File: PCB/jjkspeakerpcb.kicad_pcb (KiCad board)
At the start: 2 copper layers, 99.3 x 99.3 mm, 19 parts, among them J1 TFT 8PIN, SW1 UP, SW2 DOWN, SW3 TIME SET, SW4 CLOCK SET, SW5 SNOOZE, SW6 ALARM ON, U1 XIAO ESP32-C3

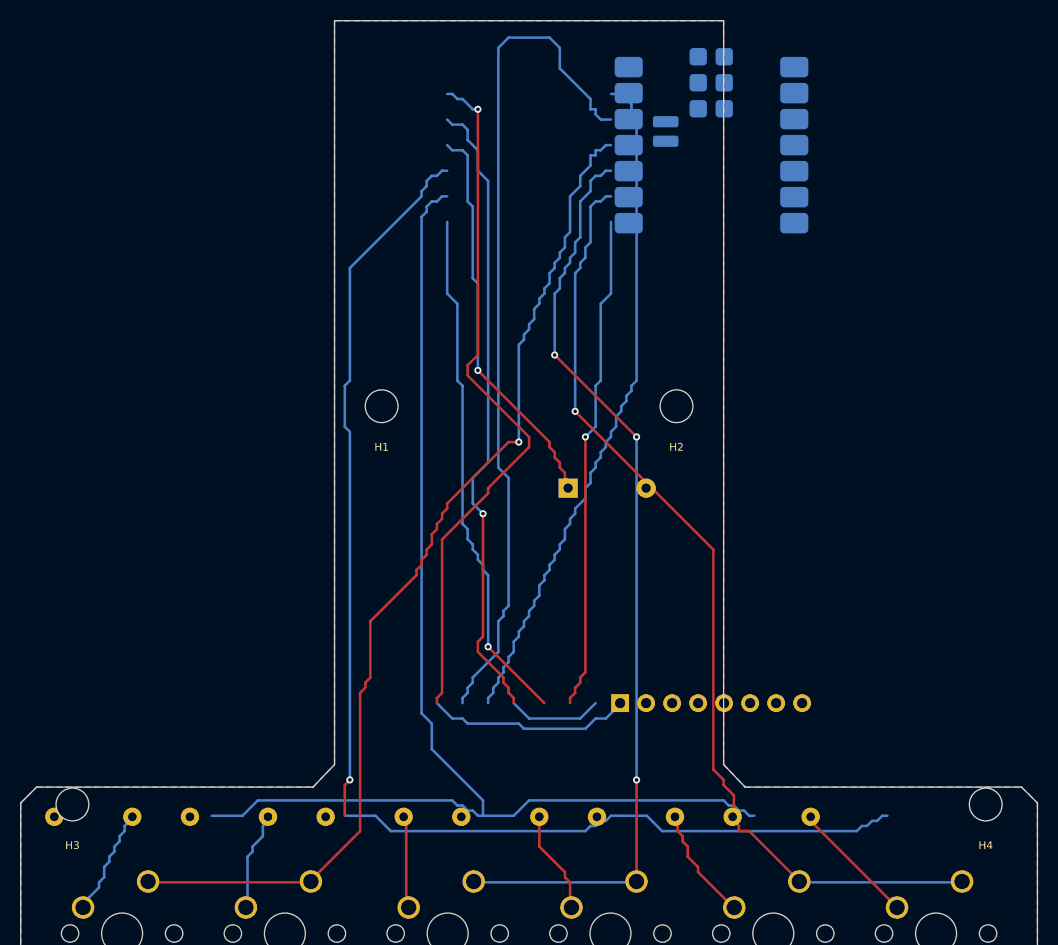
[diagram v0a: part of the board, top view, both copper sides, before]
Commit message: GGK Alarm Rev D: validated KiCad layout, firmware, safety gates and full build guide
* Add detailed native PCB parser diagnostics to Rev D audit gate

* Bisect native KiCad file parsing to identify invalid PCB S-expressions

* Repair malformed GND zone syntax and correct 1N4148 schematic orientation note

* Rebuild native KiCad from corrected B-side coordinates; remove overlapping holes, align schematic and nets

* Fix backside fab text mirror and regenerate local KiCad libraries for native ERC/DRC

* Diagnose remaining XIAO KiCad library mismatch using actual pcbnew geometry

* Reconstruct XIAO rear module from canonical front footprint with genuine mirrored SMD pads

* Isolate XIAO library shape mismatch: retain canonical 22 pad layout, remove redundant rear component graphics

* Correct underside pad mirroring; enforce native pad parity; regenerate board in CI

* Correct KiCad back-side pad positions and diode pin geometry using native observations

* Regenerate PCB and schematic using KiCad backside coordinates

* Fix XIAO local library mirroring to match audited board pad geometry

* Audit exact XIAO library footprint comparison using native pcbnew

* Regenerate PCB and schematic using KiCad backside coordinates

* Bundle XIAO as an exact native backside KiCad footprint for DRC comparison

* Regenerate PCB and schematic using KiCad backside coordinates

* Finish Rev D gate: filled GND zones, clean ERC DRC, real Arduino compile evidence

* Add no-extra-parts timer and stopwatch with overflow-safe tests and portrait UI

* Resolve native filled-zone thermal DRC at TFT J1 ground pad

* Regenerate PCB and schematic using KiCad backside coordinates

* Finalize Rev D evidence, verified BOM mounting, safe power guidance and release hold

* Retain mandatory DESIGN HOLD state while recording passing native KiCad checks

* Add native-KiCad verified design source synchronization before PR merge

* Restore known-good KiCad board generator and fix outdated Tinkercad SVG hole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
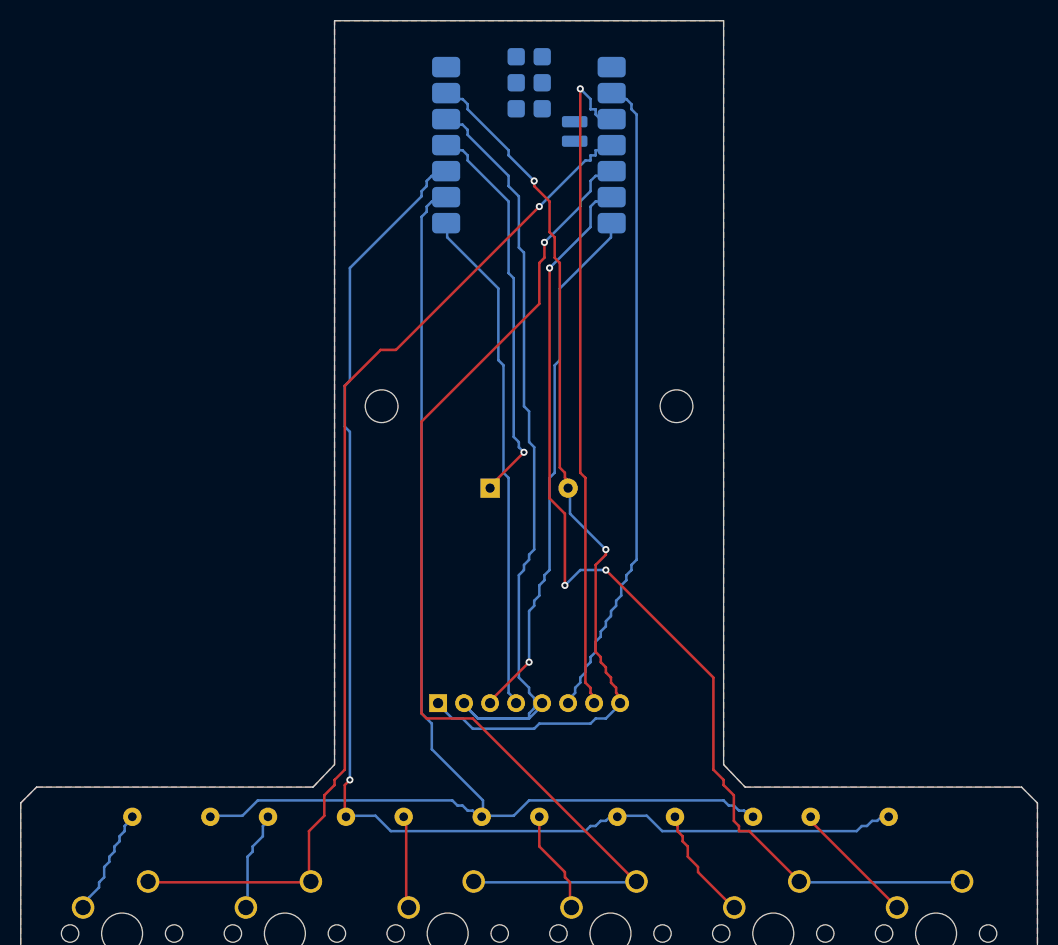
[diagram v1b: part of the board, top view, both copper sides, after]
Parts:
- removed the H1 at (35.6, 38.0)
- removed H3, H4: M3, GGK:MountingHole_3.2
- added BZ1: 3.3V PIEZO, GGK:Piezo_P12_P7.62, B.Cu at (46.2, 46.0)
- H1: renamed from BZ1; value 3.3V PIEZO -> M3; footprint GGK:Piezo_P12_P7.62 -> GGK:MountingHole_3.2; moved to F.Cu
- moved H1 19.9 mm to (35.6, 38.0)
- moved J1 17.8 mm to (41.1, 67.0)
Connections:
- net 3V3 renamed /3V3
- net COL_BOTTOM renamed /COL_BOTTOM
- net COL_MIDDLE renamed /COL_MIDDLE
- net COL_TOP renamed /COL_TOP
- net DISP_CS renamed /DISP_CS
- net DISP_DC renamed /DISP_DC
- net DISP_MOSI renamed /DISP_MOSI
- net DISP_SCK renamed /DISP_SCK
- net K1 renamed /K1
- net K2 renamed /K2
- net K3 renamed /K3
- net K4 renamed /K4
- net K5 renamed /K5
- net K6 renamed /K6
- net ROW_LEFT renamed /ROW_LEFT
- net ROW_RIGHT renamed /ROW_RIGHT
- J1 pad 1: GND -> /GND
- J1 pad 8: GND -> /GND
- U1 pad 11: PIEZO -> /PIEZO
- U1 pad 13: GND -> /GND
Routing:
- net GND: track 88.3 -> 0.00 mm, vias 1 -> 0
- net /GND: track 0.00 -> 88.0 mm, vias 0 -> 2
- net PIEZO: track 39.1 -> 0.00 mm, vias 1 -> 0
- net /PIEZO: track 0.00 -> 38.6 mm, vias 0 -> 1
- net /DISP_CS: track 83.1 -> 65.7 mm, vias 0 -> 1
- net /COL_MIDDLE: track 91.7 -> 105.1 mm, vias 3 -> 1
- net /3V3: track 71.2 -> 80.4 mm, vias 1 -> 0
- net /COL_BOTTOM: track 94.7 -> 101.3 mm, vias 1 -> 3
- net /DISP_SCK: track 48.7 -> 52.0 mm
- net /DISP_DC: track 67.1 -> 63.8 mm
- net /DISP_MOSI: track 50.9 -> 49.7 mm, vias 1 -> 0
- net /COL_TOP: track 101.2 -> 101.8 mm
- added copper zone on B.Cu, net /GND
- added copper zone on F.Cu, net /GND
- removed copper zone on B.Cu, net GND
- removed copper zone on F.Cu, net GND
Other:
- board text added: "6 KEY MATRIX / PORTRAIT TFT"
- board text added: "GGK ALARM REV D"
- board text removed: "6 KEY MATRIX // TFT ON FRONT"
- board text removed: "GGK ALARM R2"

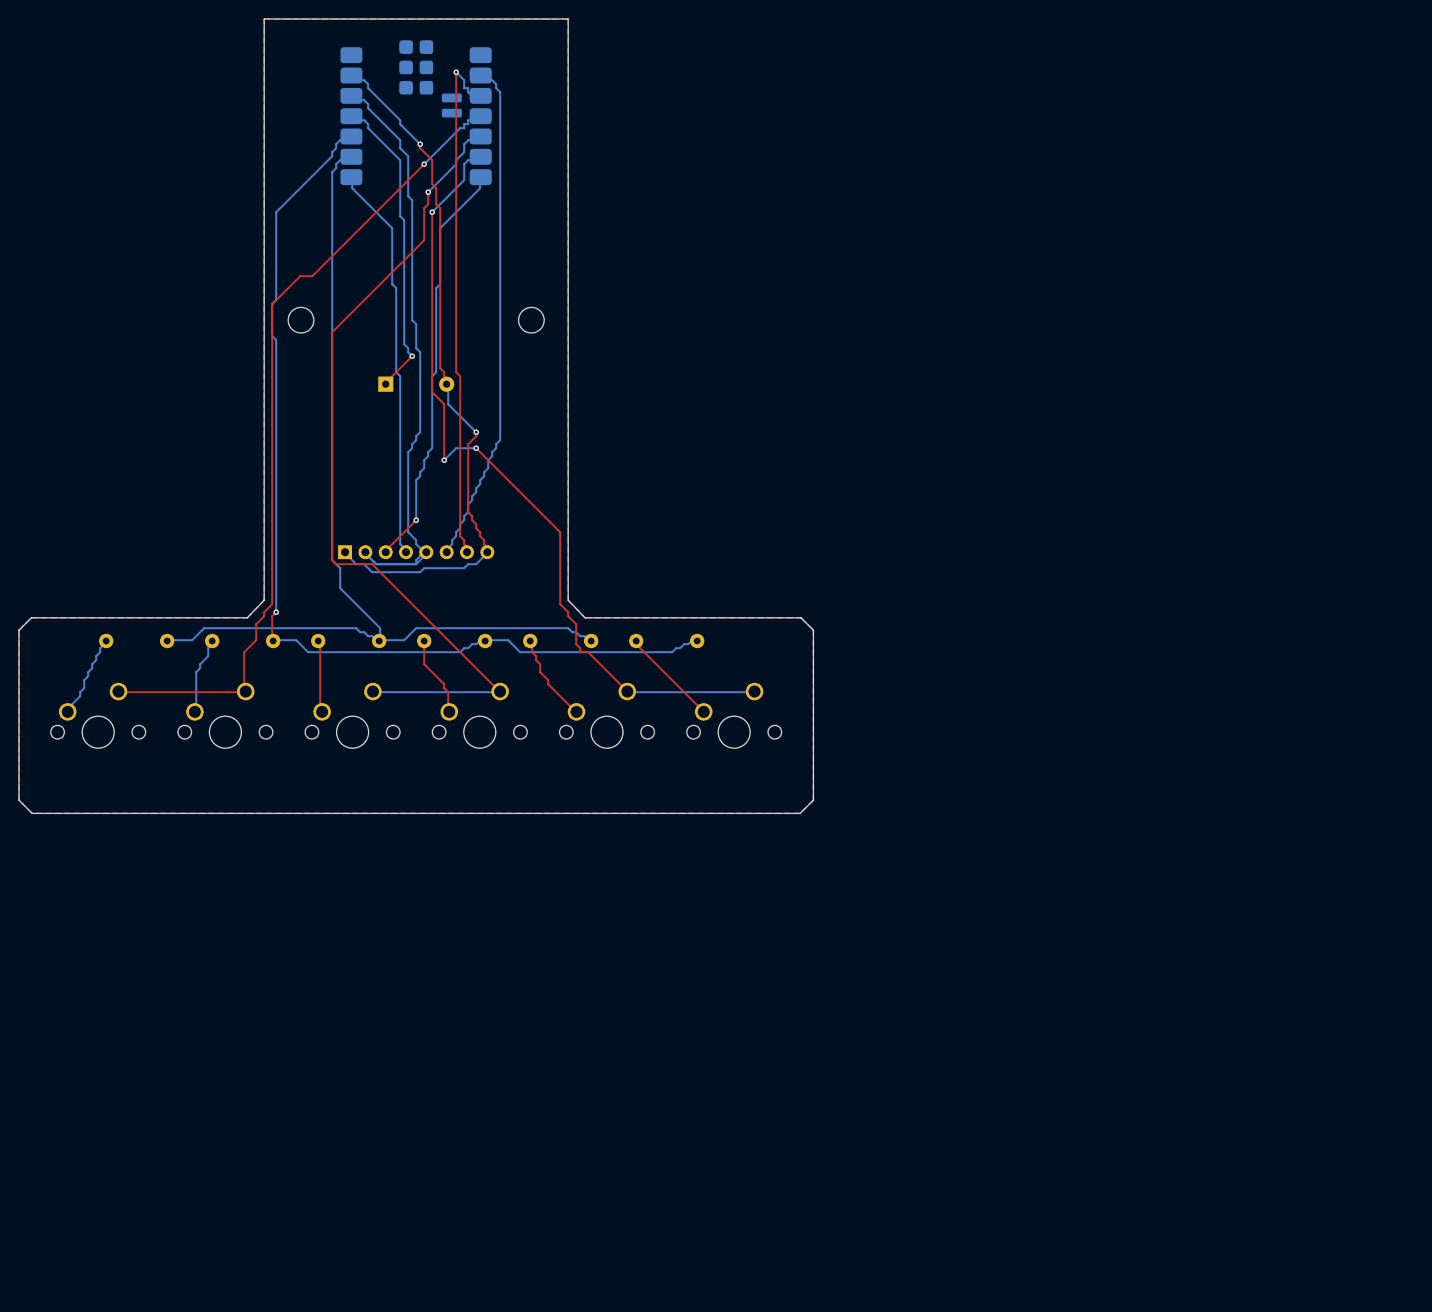
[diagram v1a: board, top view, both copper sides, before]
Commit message: Stage rectangular BLARE KiCad sources, screenshots, and incomplete Gerbers (README held)
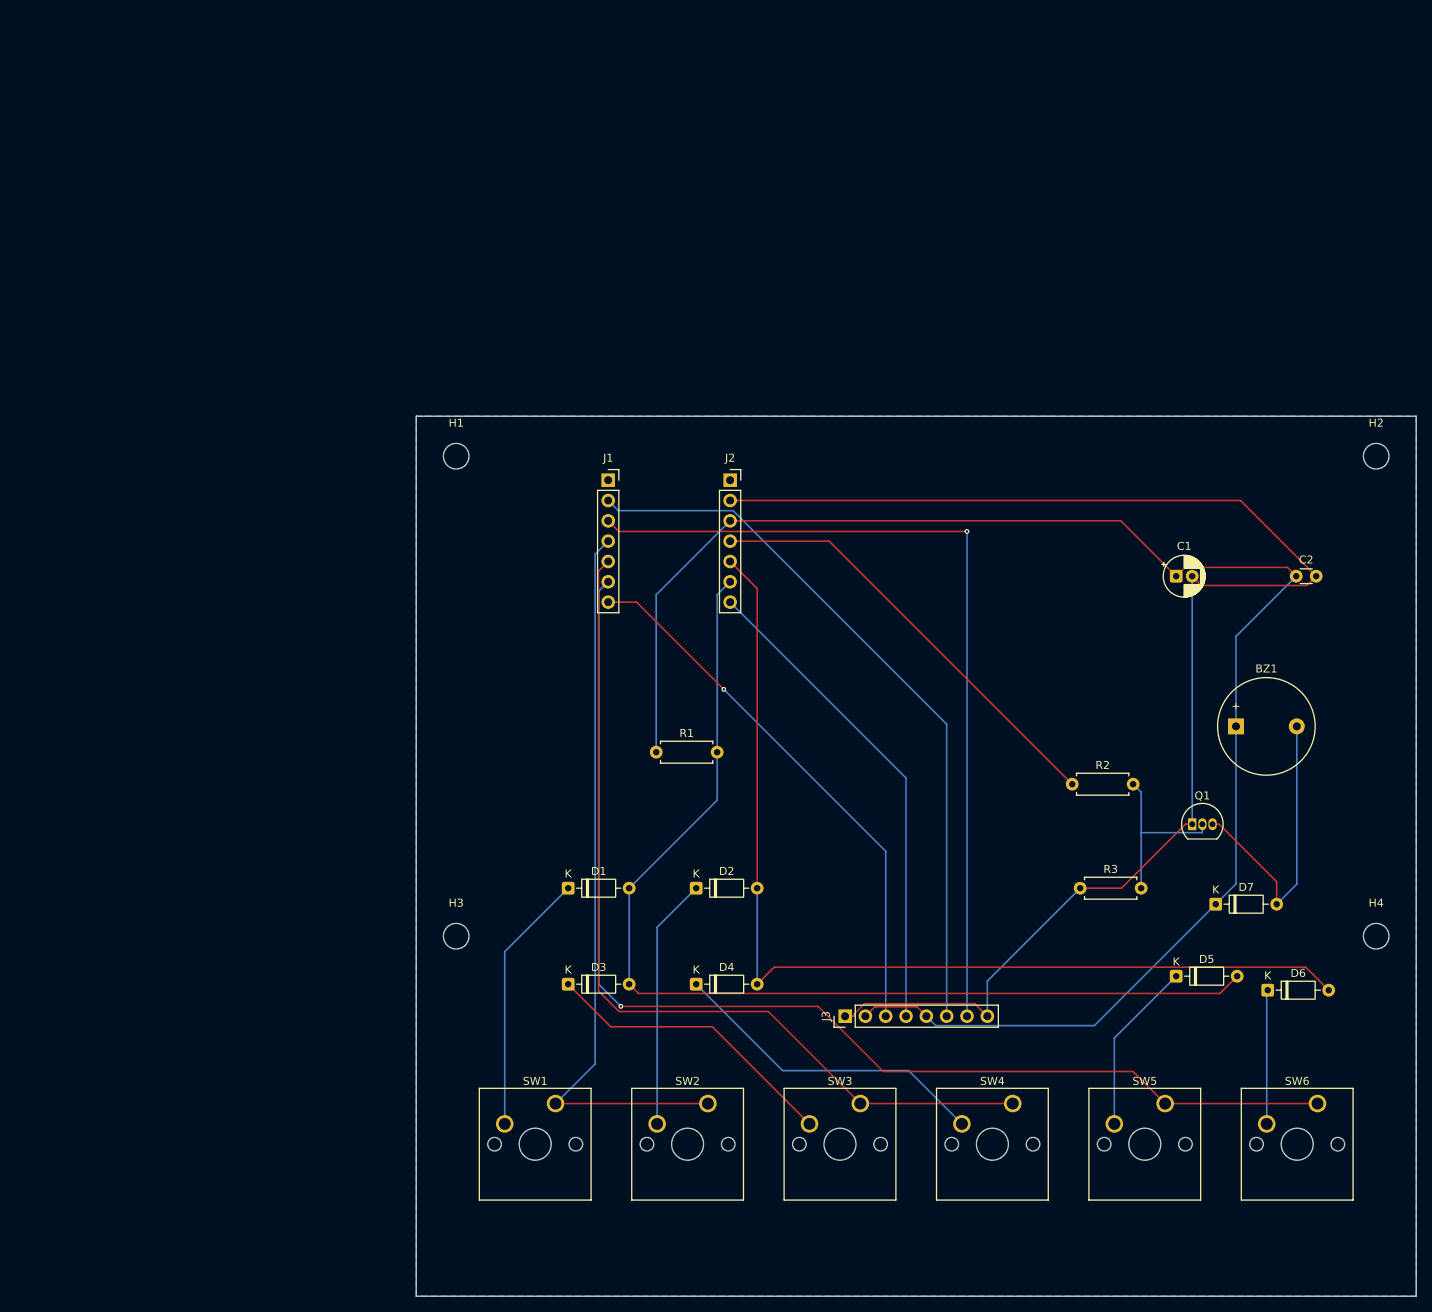
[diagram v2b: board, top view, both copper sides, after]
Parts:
- removed U1: XIAO ESP32-C3, GGK:Seeed_XIAO_ESP32C3_Castellated
- added C1: 10uF, Capacitor_THT:CP_Radial_D5.0mm_P2.00mm, F.Cu at (145.0, 70.0)
- added C2: 100nF, Capacitor_THT:C_Disc_D3.0mm_W1.6mm_P2.50mm, F.Cu at (160.0, 70.0)
- added D7: 1N4148, Diode_THT:D_DO-35_SOD27_P7.62mm_Horizontal, F.Cu at (149.9, 111.0)
- added H3: MountingHole, MountingHole:MountingHole_3.2mm_M3, F.Cu at (55.0, 115.0)
- added H4: MountingHole, MountingHole:MountingHole_3.2mm_M3, F.Cu at (170.0, 115.0)
- added J2: XIAO_RIGHT, Connector_PinSocket_2.54mm:PinSocket_1x07_P2.54mm_Vertical, F.Cu at (89.2, 58.0)
- added J3: TFT_8PIN, Connector_PinHeader_2.54mm:PinHeader_1x08_P2.54mm_Vertical, F.Cu at (103.6, 125.0)
- added Q1: 2N3904, Package_TO_SOT_THT:TO-92_Inline, F.Cu at (147.0, 101.0)
- added R1: 10k, Resistor_THT:R_Axial_DIN0207_L6.3mm_D2.5mm_P7.62mm_Horizontal, F.Cu at (80.0, 92.0)
- added R2: 1k, Resistor_THT:R_Axial_DIN0207_L6.3mm_D2.5mm_P7.62mm_Horizontal, F.Cu at (132.0, 96.0)
- added R3: 100k, Resistor_THT:R_Axial_DIN0207_L6.3mm_D2.5mm_P7.62mm_Horizontal, F.Cu at (133.0, 109.0)
- BZ1: value 3.3V PIEZO -> Buzzer_3.3V; footprint GGK:Piezo_P12_P7.62 -> Buzzer_Beeper:Buzzer_12x9.5RM7.6; moved to F.Cu
- D1, D2, D3, D4, D5, D6: footprint GGK:D_DO35_P7.62 -> Diode_THT:D_DO-35_SOD27_P7.62mm_Horizontal; moved to F.Cu
- H1, H2: value M3 -> MountingHole; footprint GGK:MountingHole_3.2 -> MountingHole:MountingHole_3.2mm_M3
- J1: value TFT 8PIN -> XIAO_LEFT; footprint GGK:PinHeader_1x08_2.54 -> Connector_PinSocket_2.54mm:PinSocket_1x07_P2.54mm_Vertical; moved to F.Cu
- SW1, SW2, SW3, SW4, SW5, SW6: footprint GGK:MX_1U_PCB -> Button_Switch_Keyboard:SW_Cherry_MX_1.00u_PCB
- moved BZ1 114.6 mm to (152.5, 88.8)
- moved H2 107.0 mm to (170.0, 55.0)
- moved D5 91.0 mm to (145.0, 120.0)
- moved D6 90.2 mm to (156.4, 121.8)
- moved SW6 87.2 mm to (162.7, 135.9)
- moved SW5 84.7 mm to (143.6, 135.9)
- moved SW4 82.2 mm to (124.6, 135.9)
- moved SW3 79.8 mm to (105.5, 135.9)
- moved SW2 77.4 mm to (86.5, 135.9)
- moved SW1 75.1 mm to (67.4, 135.9)
- moved D2 67.9 mm to (85.0, 109.0)
- moved D1 65.5 mm to (69.0, 109.0)
- moved D4 54.7 mm to (85.0, 121.0)
- moved D3 53.1 mm to (69.0, 121.0)
- moved J1 34.1 mm to (74.0, 58.0)
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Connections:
- net /K1 renamed Net-(D1-K)
- net /K2 renamed Net-(D2-K)
- net /K3 renamed Net-(D3-K)
- net /K4 renamed Net-(D4-K)
- net /K5 renamed Net-(D5-K)
- net /K6 renamed Net-(D6-K)
- net /ROW_LEFT renamed /LEFT
- net /ROW_RIGHT renamed /RIGHT
- BZ1 pad 1: /PIEZO -> +3V3
- BZ1 pad 2: /GND -> /NEG
- J1 pad 1: /GND -> unconnected-(J1-Pin_1-Pad1)
- J1 pad 2: /3V3 -> /DC
- J1 pad 3: /DISP_SCK -> /CS
- J1 pad 4: /DISP_MOSI -> /TOP
- J1 pad 5: /3V3 -> /MID
- J1 pad 6: /DISP_DC -> /BOT
- J1 pad 7: /DISP_CS -> /DISP_SCK
- SW1 pad 1: /COL_TOP -> /TOP
- SW2 pad 1: /COL_TOP -> /TOP
- SW3 pad 1: /COL_MIDDLE -> /MID
- SW4 pad 1: /COL_MIDDLE -> /MID
- SW5 pad 1: /COL_BOTTOM -> /BOT
- SW6 pad 1: /COL_BOTTOM -> /BOT
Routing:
- net +3V3: track 0.00 -> 204.0 mm
- net GND: track 0.00 -> 182.0 mm
- net /BOT: track 0.00 -> 146.8 mm, vias 0 -> 1
- net /MID: track 0.00 -> 111.8 mm
- net /CS: track 0.00 -> 106.0 mm, vias 0 -> 1
- net /COL_MIDDLE: track 105.1 -> 0.00 mm, vias 1 -> 0
- net /COL_TOP: track 101.8 -> 0.00 mm, vias 1 -> 0
- net /COL_BOTTOM: track 101.3 -> 0.00 mm, vias 3 -> 0
- net /TOP: track 0.00 -> 92.1 mm
- net /DC: track 0.00 -> 90.4 mm
- net /GND: track 88.0 -> 0.00 mm, vias 2 -> 0
- net /3V3: track 80.4 -> 0.00 mm
- net /DISP_CS: track 65.7 -> 0.00 mm, vias 1 -> 0
- net /DISP_DC: track 63.8 -> 0.00 mm
- net /10: track 0.00 -> 55.3 mm
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- added copper zone on B.Cu, net GND
- removed copper zone on B.Cu, net /GND
- removed copper zone on F.Cu, net /GND
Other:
- board size 99.3 x 99.3 mm -> 125 x 110 mm
- board text removed: "6 KEY MATRIX / PORTRAIT TFT"
- board text removed: "GGK ALARM REV D"
- board text removed: "PORTRAIT TFT REF ONLY 21.08 X 73.15 MM"
